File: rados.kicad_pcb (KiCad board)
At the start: 2 copper layers, 156 parts, among them J1 HEADER, J10 STEPSTICK, J11 STEPSTICK, J12 STEPSTICK, J13 MICROSD_SLOT_TFP09-2-12B, J2 HEADER, J3 HEADER, J4 STEPSTICK, J5 STEPSTICK, J6 STEPSTICK, J7 HEADER, J8 HEADER, J9 HEADER, P1 CONN_01X02, P10 CONN_01X04, P11 CONN_01X04, P12 CONN_01X04, P13 EXT_SD, P14 LCD, P15 LIMIT_SWITCHES, P16 LIMIT_SWITCHES_V, P17 CONN_01X03, P18 CONN_01X03, P19 CONN_01X03, P2 CONN_01X02, P20 CONN_01X03, P21 THERMISTORS, P22 CONN_01X05, P3 CONN_01X02, P4 CONN_01X02, P5 HP_MOSFETS, P6 MP_MOSFETS, P7 CONN_02X04, P8 CONN_01X04, P9 CONN_01X04, Q1 2N7002P, Q10 2N7002P, Q11 2N7002P, Q12 BC846BPDW1, Q13 BC846BPDW1, Q14 SI2318CDS-T1-GE3, Q15 IRFB7545PbF, Q16 2N7002P, Q17 2N7002P, Q18 BC846BPDW1, Q19 BC846BPDW1, Q2 2N7002P, Q20 SI2318CDS-T1-GE3, Q21 IRFB7545PbF, Q3 2N7002P, Q4 BC846BPDW1, Q5 BC846BPDW1, Q6 BC846BPDW1, Q7 IRFB7545PbF, Q8 SI2318CDS-T1-GE3, Q9 IRFB7545PbF, SW1 RESET, U1 MC34063, U2 24LC256

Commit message: More routing
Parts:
- added C33: 10uF, Capacitors_SMD:C_0805, F.Cu at (112.5, 140.1)
- C12, C13, C14, C15, C16, C17: footprint geda-footprints:ELCO-8mm -> armin-footprints:ELCO-8mm
- D10, D13, D14, D17, D3, D4, D5, D9: footprint geda-footprints:0603diode -> armin-footprints:0603diode
- D11, D15, D7: footprint geda-footprints:LL-34 -> armin-footprints:LL-34
- D12, D16, D2, D6, D8: footprint geda-footprints:DO214AC -> armin-footprints:DO214AC
- L1: value 100uF -> 100uH
- Q1, Q10, Q11, Q14, Q16, Q17, Q2, Q20, Q3, Q8: footprint geda-footprints:SOT23_3L -> armin-footprints:SOT23_3L
- Q12, Q13, Q18, Q19, Q4, Q5, Q6: footprint geda-footprints:SC70_6L -> armin-footprints:SC70_6L
- Q15, Q21, Q7, Q9: footprint geda-footprints:TO-220 -> armin-footprints:TO-220
- R10: value 1K8 -> 4K7; footprint Resistors_SMD:R_0603 -> Resistors_SMD:R_0805
- U1, U2: footprint geda-footprints:SOIC8 -> armin-footprints:SOIC8
- moved D10 179.5 mm to (96.0, 75.2), turned to 90 degrees
- moved D14 177.1 mm to (96.0, 64.2), turned to 90 degrees
- moved Q17 176.6 mm to (99.0, 65.0), turned to 180 degrees
- moved R23 176.6 mm to (96.2, 71.8), turned to 90 degrees
- moved Q19 174.9 mm to (98.9, 61.4), turned to 180 degrees
- moved R31 173.3 mm to (96.3, 60.9), turned to 90 degrees
- moved Q4 173.2 mm to (98.8, 95.3), turned to 180 degrees
- moved Q11 171.0 mm to (99.0, 76.3), turned to 180 degrees
- moved R29 171.0 mm to (96.2, 67.5), turned to 90 degrees
- moved C5 169.7 mm to (95.9, 56.5), turned to 90 degrees
- moved D3 167.1 mm to (96.0, 97.5), turned to 90 degrees
- moved R27 166.5 mm to (98.9, 59.2)
- moved Q1 165.3 mm to (99.0, 98.2), turned to 180 degrees
- moved C11 161.4 mm to (101.2, 61.2), turned to 90 degrees
- moved R5 161.2 mm to (101.0, 56.5), turned to 270 degrees
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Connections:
- net LCD-5 renamed Net-(SHIELD1-Pad45)
- net LCD-7 renamed Net-(SHIELD1-Pad47)
- J1 pad 2: Net-(J1-Pad2) -> +3V3
- J1 pad 4: Net-(J1-Pad4) -> +3V3
- J1 pad 6: Net-(J1-Pad6) -> +3V3
- J11 pad 1: E1-EN -> E2-EN
- J11 pad 7: E1-STEP -> E2-STEP
- J11 pad 8: E1-DIR -> E2-DIR
- J12 pad 1: E2-EN -> E1-EN
- J12 pad 7: E2-STEP -> E1-STEP
- J12 pad 8: E2-DIR -> E1-DIR
- J2 pad 2: Net-(J2-Pad2) -> +3V3
- J2 pad 4: Net-(J2-Pad4) -> +3V3
- J2 pad 6: Net-(J2-Pad6) -> +3V3
- J3 pad 2: Net-(J3-Pad2) -> +3V3
- J3 pad 4: Net-(J3-Pad4) -> +3V3
- J3 pad 6: Net-(J3-Pad6) -> +3V3
- J4 pad 2: Net-(J1-Pad2) -> Net-(J1-Pad1)
- J4 pad 3: Net-(J1-Pad4) -> Net-(J1-Pad3)
- J4 pad 4: Net-(J1-Pad6) -> Net-(J1-Pad5)
- J5 pad 2: Net-(J2-Pad2) -> Net-(J2-Pad1)
- J5 pad 3: Net-(J2-Pad4) -> Net-(J2-Pad3)
- J5 pad 4: Net-(J2-Pad6) -> Net-(J2-Pad5)
- J6 pad 2: Net-(J3-Pad2) -> Net-(J3-Pad1)
- J6 pad 3: Net-(J3-Pad4) -> Net-(J3-Pad3)
- J6 pad 4: Net-(J3-Pad6) -> Net-(J3-Pad5)
- J7 pad 1: Net-(J7-Pad1) -> Net-(J10-Pad2)
- J7 pad 2: Net-(J10-Pad2) -> +3V3
- J7 pad 3: Net-(J7-Pad3) -> Net-(J10-Pad3)
- J7 pad 4: Net-(J10-Pad3) -> +3V3
- J7 pad 5: Net-(J7-Pad5) -> Net-(J10-Pad4)
- J7 pad 6: Net-(J10-Pad4) -> +3V3
- J8 pad 1: Net-(J8-Pad1) -> Net-(J11-Pad2)
- J8 pad 2: Net-(J11-Pad2) -> +3V3
- J8 pad 3: Net-(J8-Pad3) -> Net-(J11-Pad3)
- J8 pad 4: Net-(J11-Pad3) -> +3V3
- J8 pad 5: Net-(J8-Pad5) -> Net-(J11-Pad4)
- J8 pad 6: Net-(J11-Pad4) -> +3V3
- J9 pad 1: Net-(J9-Pad1) -> Net-(J12-Pad2)
- J9 pad 2: Net-(J12-Pad2) -> +3V3
- J9 pad 3: Net-(J9-Pad3) -> Net-(J12-Pad3)
- J9 pad 4: Net-(J12-Pad3) -> +3V3
- J9 pad 5: Net-(J9-Pad5) -> Net-(J12-Pad4)
- J9 pad 6: Net-(J12-Pad4) -> +3V3
- P17 pad 1: GND -> +3V3
- P17 pad 2: +3V3 -> GND
- P18 pad 1: GND -> +3V3
- P18 pad 2: +3V3 -> GND
- P19 pad 1: GND -> +3V3
- P19 pad 2: +3V3 -> GND
- P20 pad 1: GND -> +3V3
- P20 pad 2: +3V3 -> GND
- R35 pad 1: Net-(R35-Pad1) -> +3V3
- R36 pad 1: Net-(R35-Pad1) -> +3V3
- SHIELD1 pad 0: Y-STEP -> HP-FET3
- SHIELD1 pad 1: Net-(SHIELD1-Pad1) -> Y-STEP
- SHIELD1 pad 15: Net-(SHIELD1-Pad15) -> MP-FET1
- SHIELD1 pad 16: Y-DIR -> LP-FET1
- SHIELD1 pad 17: MP-FET1 -> LP-FET2
- SHIELD1 pad 18: LP-FET2 -> X-STEP
- SHIELD1 pad 19: LP-FET1 -> X-DIR
- SHIELD1 pad 2: Net-(SHIELD1-Pad2) -> Y-DIR
- SHIELD1 pad 22: Y-EN -> X-
- SHIELD1 pad 23: X-DIR -> X+
- SHIELD1 pad 24: X-STEP -> Y-
- SHIELD1 pad 25: Net-(SHIELD1-Pad25) -> Y+
- SHIELD1 pad 26: X-EN -> Z-
- SHIELD1 pad 27: Net-(SHIELD1-Pad27) -> Z+
- SHIELD1 pad 28: X- -> PROBE
- SHIELD1 pad 29: Net-(SHIELD1-Pad29) -> STATUS-LED
- SHIELD1 pad 3: Net-(SHIELD1-Pad3) -> Y-EN
- SHIELD1 pad 30: Y- -> Net-(SHIELD1-Pad30)
- SHIELD1 pad 32: Z- -> Net-(SHIELD1-Pad32)
- SHIELD1 pad 33: Net-(SHIELD1-Pad33) -> LCD-D4
- SHIELD1 pad 34: X+ -> LCD-D7
- SHIELD1 pad 35: Net-(SHIELD1-Pad35) -> LCD-D6
- SHIELD1 pad 36: Y+ -> LCD-E
- SHIELD1 pad 37: Net-(SHIELD1-Pad37) -> LCD-D5
- SHIELD1 pad 38: Z+ -> LCD-RS
- SHIELD1 pad 39: Net-(SHIELD1-Pad39) -> ENC-B
- SHIELD1 pad 40: Net-(SHIELD1-Pad40) -> X-EN
- SHIELD1 pad 41: STATUS-LED -> ENC-A
- SHIELD1 pad 42: LCD-RS -> E3-EN
- SHIELD1 pad 43: LCD-E -> Net-(SHIELD1-Pad43)
- SHIELD1 pad 44: LCD-4 -> E3-STEP
- SHIELD1 pad 46: LCD-6 -> E3-DIR
- SHIELD1 pad 49: E3-EN -> Net-(SHIELD1-Pad49)
- SHIELD1 pad 50: ENC-B -> Net-(SHIELD1-Pad50)
- SHIELD1 pad 51: E3-STEP -> Net-(SHIELD1-Pad51)
- SHIELD1 pad 52: ENC-A -> Net-(SHIELD1-Pad52)
- SHIELD1 pad 53: E3-DIR -> Net-(SHIELD1-Pad53)
- SHIELD1 pad 7: HP-FET3 -> Net-(SHIELD1-Pad7)
- SHIELD1 pad AD0: Net-(SHIELD1-PadAD0) -> E1-DIR
- SHIELD1 pad AD1: Net-(SHIELD1-PadAD1) -> E1-STEP
- SHIELD1 pad AD10: E2-STEP -> AUX-4
- SHIELD1 pad AD11: T4 -> T0
- SHIELD1 pad AD12: T3 -> T1
- SHIELD1 pad AD14: T1 -> T3
- SHIELD1 pad AD15: T0 -> T4
- SHIELD1 pad AD2: Net-(SHIELD1-PadAD2) -> E1-EN
- SHIELD1 pad AD3: Net-(SHIELD1-PadAD3) -> E2-DIR
- SHIELD1 pad AD4: Net-(SHIELD1-PadAD4) -> E2-STEP
- SHIELD1 pad AD6: E1-DIR -> Net-(SHIELD1-PadAD6)
- SHIELD1 pad AD7: E1-STEP -> AUX-1
- SHIELD1 pad AD8: E1-EN -> AUX-2
- SHIELD1 pad AD9: E2-DIR -> AUX-3
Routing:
- net +3V3: track 0.00 -> 373.8 mm
- net +12V: track 26.5 -> 185.7 mm
- net SD2-CS: track 0.00 -> 81.1 mm
- net E1-DIR: track 0.00 -> 61.3 mm
- net E1-STEP: track 0.00 -> 61.1 mm
- net Vsupply: track 261.0 -> 321.8 mm
- net E1-EN: track 0.00 -> 48.5 mm
- net E3-EN: track 0.00 -> 45.3 mm
- net AUX-1: track 0.00 -> 41.6 mm
- net +5V: track 0.00 -> 39.1 mm
- net E2-EN: track 0.00 -> 37.3 mm
- net AUX-2: track 0.00 -> 36.9 mm
- net AUX-3: track 0.00 -> 32.6 mm
- net STATUS-LED: track 0.00 -> 29.2 mm
- net AUX-4: track 0.00 -> 29.2 mm
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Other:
- board outline added: 83 x 106 mm
- net class Default: clearance 0.15 -> 0.1524; trace_width 0.15 -> 0.1524
- rule trace_clearance: 0.15 -> 0.1524
- rule trace_min: 0.15 -> 0.1524

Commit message: Routing almost finished
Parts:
- removed R32, R33, R34: 10K, Resistors_SMD:R_0603
- moved C33 116.4 mm to (92.4, 25.4), turned to 180 degrees
- moved C31 26.7 mm to (149.2, 99.0), turned to 180 degrees
- moved C18 19.5 mm to (142.6, 112.9), turned to 180 degrees
- moved JP2 6.39 mm to (152.3, 105.9), turned to 180 degrees
- moved C32 1.23 mm to (107.0, 106.3)
- moved R42 1.03 mm to (92.8, 27.4), turned to 180 degrees
- moved J13 0.75 mm to (140.0, 118.3)
- moved C30 0.45 mm to (151.4, 33.0)
- moved R6 0.40 mm to (100.8, 89.4)
- moved SW1 0.16 mm to (133.2, 127.5)
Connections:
- C31 pad 2: Net-(C31-Pad2) -> GND
- SHIELD1 pad 1: Y-STEP -> Y-EN
- SHIELD1 pad 3: Y-EN -> Y-STEP
- SHIELD1 pad 42: E3-EN -> Net-(SHIELD1-Pad42)
- SHIELD1 pad 44: E3-STEP -> E3-EN
- SHIELD1 pad 45: Net-(SHIELD1-Pad45) -> E3-STEP
- SHIELD1 pad 48: ENC-SW -> Net-(SHIELD1-Pad48)
- SHIELD1 pad 7: Net-(SHIELD1-Pad7) -> HP-FET1
- SHIELD1 pad 8: HP-FET1 -> Z-STEP
- SHIELD1 pad 9: Z-STEP -> ENC-SW
- SW1 pad 2: Net-(C31-Pad2) -> GND
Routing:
- net +3V3: track 373.8 -> 531.7 mm, vias 0 -> 3
- net SD-CS: track 0.00 -> 77.6 mm
- net Net-(D2-Pad1): track 0.00 -> 71.4 mm
- net RESET: track 0.00 -> 48.9 mm
- net ENC-SW: track 0.00 -> 48.9 mm
- net +12V: track 185.7 -> 230.0 mm
- net SD-SCK: track 48.5 -> 83.9 mm
- net SD-MOSI: track 51.7 -> 86.5 mm, vias 0 -> 1
- net SD-MISO: track 53.1 -> 85.2 mm
- net GND: track 51.7 -> 75.7 mm, vias 22 -> 32
- net ARDUINO-VIN: track 0.00 -> 21.7 mm
- net Z-EN: track 24.5 -> 36.3 mm
- net Y-STEP: track 0.00 -> 5.82 mm
- net Net-(Q7-Pad1): track 0.00 -> 4.89 mm
- net LP-OUT1: track 9.13 -> 13.6 mm
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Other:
- board size 83 x 106 mm -> 83.2 x 106 mm

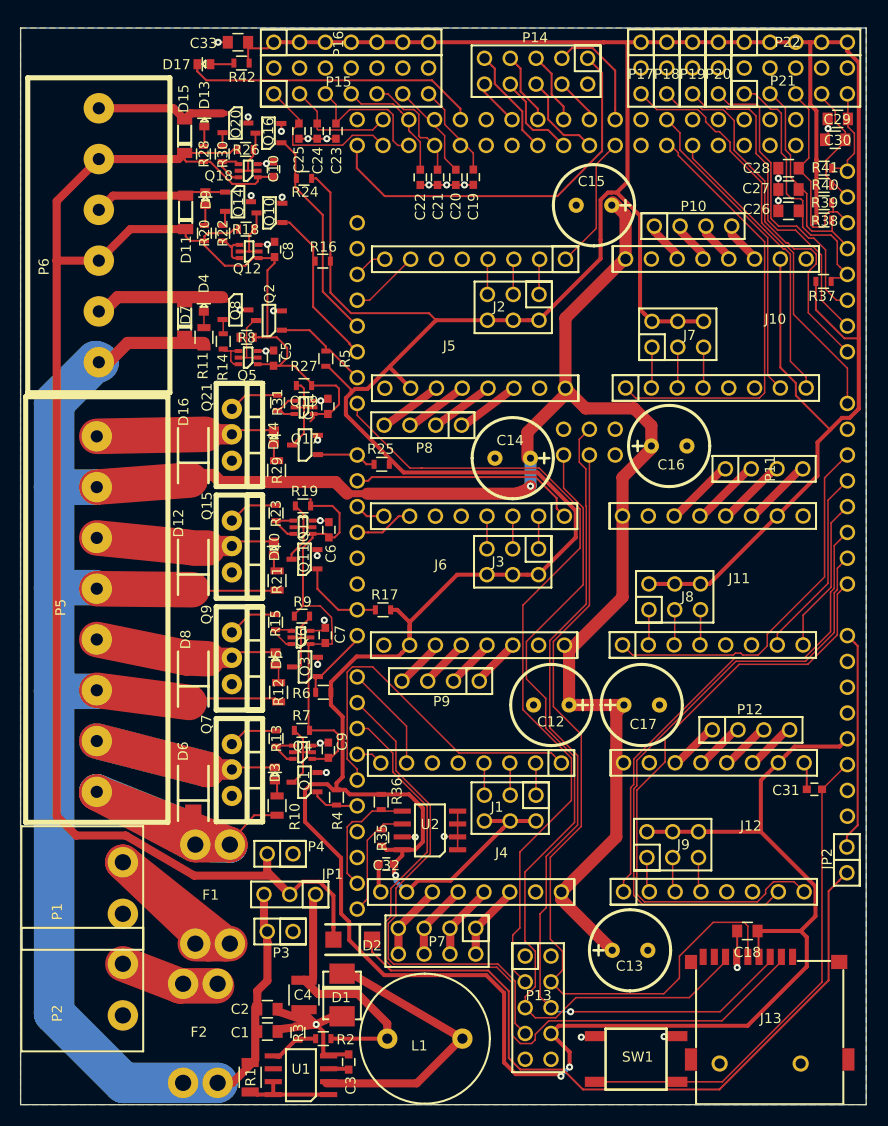
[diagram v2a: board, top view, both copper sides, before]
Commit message: Added 3d models
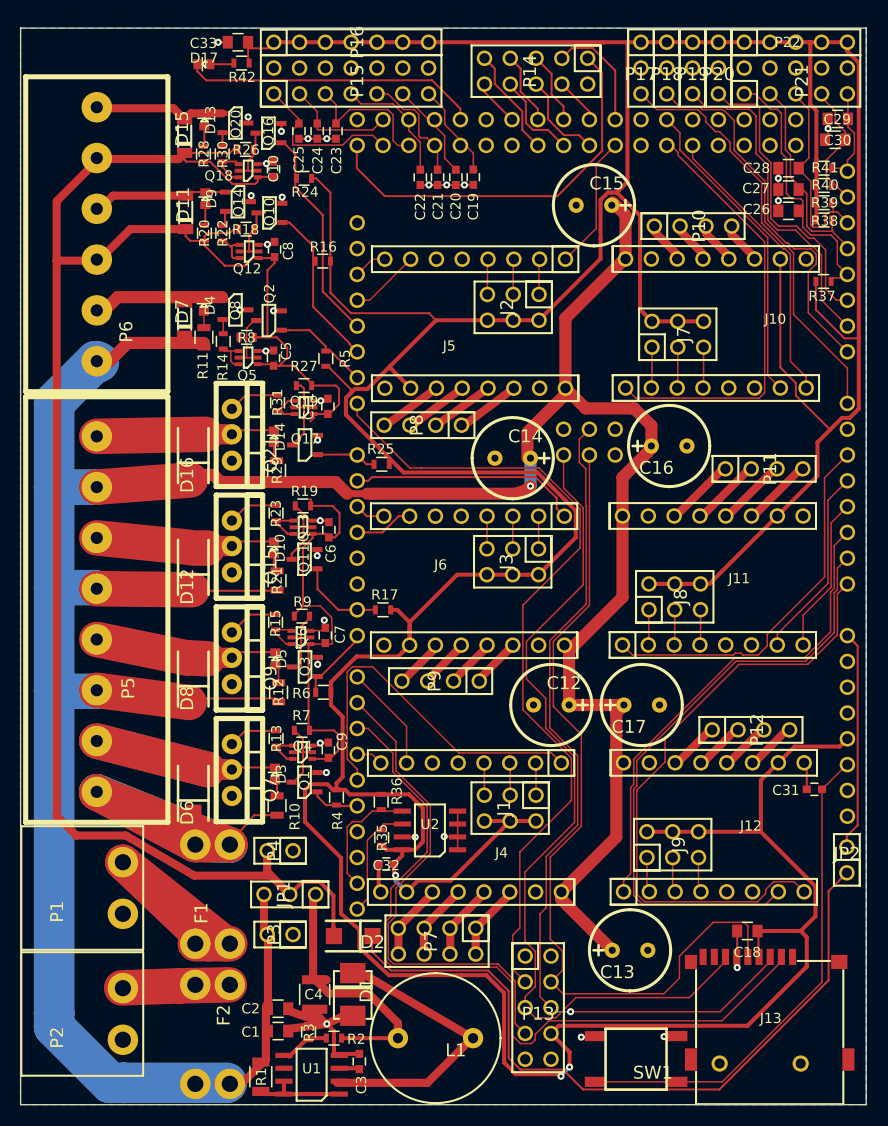
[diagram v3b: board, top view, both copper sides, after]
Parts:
- D1: footprint geda-footprints:SMB -> armin-footprints:DO214AA
- F1, F2: footprint geda-footprints:FUSEHOLDER_MINI_KEYSTONE_3557 -> armin-footprints:FUSEHOLDER_MINI_KEYSTONE_3557
- J1, J2, J3, J7, J8, J9: footprint geda-footprints:CON_HDR_2x3 -> armin-footprints:CON_HDR_2x3_2.54mm
- JP1, P17, P18, P19, P20: footprint geda-footprints:CON_HDR_1x3 -> armin-footprints:CON_HDR_1x3_2.54mm
- JP2, P3, P4: footprint geda-footprints:CON_HDR_1x2 -> armin-footprints:CON_HDR_1x2_2.54mm
- L1: footprint geda-footprints:INDUCTOR_AIUR06 -> armin-footprints:INDUCTOR_AIUR06
- P1, P2: footprint geda-footprints:CON_WURTH_WR_TBL_313_2 -> armin-footprints:CON_PHOENIX_MSTBA-2.5-2-G-5.08
- P10, P11, P12, P8, P9: footprint geda-footprints:CON_HDR_1x4 -> armin-footprints:CON_HDR_1x4_2.54mm
- P13, P14, P21: footprint geda-footprints:CON_HDR_2x5 -> armin-footprints:CON_HDR_2x5_2.54mm
- P15: footprint geda-footprints:CON_HDR_2x7 -> armin-footprints:CON_HDR_2x7_2.54mm
- P16: footprint geda-footprints:CON_HDR_1x7 -> armin-footprints:CON_HDR_1x7_2.54mm
- P5: footprint geda-footprints:CON_SCRW_8_PIN_5mm -> armin-footprints:TERMINAL_BLOCK_8_PIN_5mm
- P6: footprint geda-footprints:CON_SCRW_6_PIN_5mm -> armin-footprints:TERMINAL_BLOCK_6_PIN_5mm
- P7: footprint geda-footprints:CON_HDR_2x4 -> armin-footprints:CON_HDR_2x4_2.54mm
- SW1: footprint geda-footprints:BUTTON_PUSH_SMD_6x6mm -> armin-footprints:BUTTON_PUSH_SMD_6x6mm
- moved P2 2.40 mm to (74.0, 123.4)
- moved F2 1.20 mm to (91.6, 121.2)
- moved R1 1.05 mm to (94.7, 127.2)
- moved U1 1.05 mm to (99.7, 127.0)
- moved R3 1.05 mm to (99.3, 122.8)
- moved C1 1.05 mm to (96.3, 122.8)
- moved C2 1.05 mm to (96.3, 120.5)
- moved C3 1.05 mm to (104.3, 125.8)
- moved C4 1.05 mm to (100.0, 119.2)
- moved D1 1.05 mm to (104.5, 118.8)
- moved L1 1.05 mm to (113.8, 125.2)
- moved R2 1.05 mm to (101.8, 123.5)
- moved D2 0.35 mm to (105.7, 113.4)
- moved P3 0.30 mm to (96.5, 113.2)
- moved P4 0.30 mm to (96.5, 105.0)
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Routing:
- net Vsupply: track 318.9 -> 320.3 mm
- net Net-(F2-Pad1): track 9.63 -> 10.6 mm

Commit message: More 3d stuff
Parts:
- added C34: 10uF, Capacitors_SMD:C_0805, F.Cu at (104.3, 39.1)
- C4: footprint Resistors_SMD:R_1210 -> Capacitors_SMD:C_1210
- J10, J11, J12, J4, J5, J6: footprint geda-footprints:STEPSTICK -> armin-footprints:STEPSTICK
- P22: footprint geda-footprints:CON_HDR_1x5 -> armin-footprints:CON_HDR_1x5_2.54mm
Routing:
- net +5V: track 39.0 -> 39.8 mm, vias 0 -> 1

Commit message: More 3d stuff
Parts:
- C1, C18, C2, C26, C27, C28, C29, C30, C33, C34: footprint Capacitors_SMD:C_0805 -> capacitors:C_0805
- C10, C11, C19, C20, C21, C22, C23, C24, C25, C3, C31, C32, C5, C6, C7, C8, C9: footprint Capacitors_SMD:C_0603 -> capacitors:C_0603
- C12, C13, C14, C15, C16, C17: footprint armin-footprints:ELCO-8mm -> capacitors:ELCO-8mm-3.5mm_pitch
- C4: footprint Capacitors_SMD:C_1210 -> capacitors:C_1210
- D1: footprint armin-footprints:DO214AA -> diodes:DO214AA_SMB
- D10, D13, D14, D17, D3, D4, D5, D9: footprint armin-footprints:0603diode -> diodes:LED-0603
- D11, D15, D7: footprint armin-footprints:LL-34 -> diodes:SOD-80C
- D12, D16, D2, D6, D8: footprint armin-footprints:DO214AC -> diodes:DO214AC_SMA
- F1, F2: footprint armin-footprints:FUSEHOLDER_MINI_KEYSTONE_3557 -> misc:FUSEHOLDER_MINI_KEYSTONE_3557
- L1: footprint armin-footprints:INDUCTOR_AIUR06 -> inductors:INDUCTOR_AIUR06
- P1, P2: footprint armin-footprints:CON_PHOENIX_MSTBA-2.5-2-G-5.08 -> terminal_blocks:CON_PHOENIX_MSTBA-2.5-2-G-5.08
- P5: footprint armin-footprints:TERMINAL_BLOCK_8_PIN_5mm -> terminal_blocks:TERMINAL_BLOCK_8_PIN_5mm
- P6: footprint armin-footprints:TERMINAL_BLOCK_6_PIN_5mm -> terminal_blocks:TERMINAL_BLOCK_6_PIN_5mm
- Q1, Q10, Q11, Q14, Q16, Q17, Q2, Q20, Q3, Q8: footprint armin-footprints:SOT23_3L -> sot:SOT23_3L
- Q12, Q13, Q18, Q19, Q4, Q5, Q6: footprint armin-footprints:SC70_6L -> sot:SC70_6L
- Q15, Q21, Q7, Q9: footprint armin-footprints:TO-220 -> to:TO-220
- R1: footprint Resistors_SMD:R_1206 -> resistors:R_1206
- R10, R11, R12, R21, R29: footprint Resistors_SMD:R_0805 -> resistors:R_0805
- R13, R14, R15, R16, R17, R18, R19, R2, R20, R22, R23, R24, R25, R26, R27, R28, R3, R30, R31, R35, R36, R37, R38, R39, R4, R40, R41, R42, R5, R6, R7, R8, R9: footprint Resistors_SMD:R_0603 -> resistors:R_0603
- SW1: footprint armin-footprints:BUTTON_PUSH_SMD_6x6mm -> buttons_switches:BUTTON_PUSH_SMD_6x6mm
- U1, U2: footprint armin-footprints:SOIC8 -> soic:SOIC8
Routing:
- net +5V: track 39.8 -> 4.98 mm
- net GND: track 75.7 -> 110.5 mm

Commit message: cleanup
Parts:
- Q15, Q21, Q7, Q9: footprint to:TO-220 -> to:TO-220-3

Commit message: fixed minor issue
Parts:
- J1, J2, J3, J7, J8, J9: footprint armin-footprints:CON_HDR_2x3_2.54mm -> headers:CON_HDR_2x3_2.54mm
- JP1, P17, P18, P19, P20: footprint armin-footprints:CON_HDR_1x3_2.54mm -> headers:CON_HDR_1x3_2.54mm
- JP2, P3, P4: footprint armin-footprints:CON_HDR_1x2_2.54mm -> headers:CON_HDR_1x2_2.54mm
- P10, P11, P12, P8, P9: footprint armin-footprints:CON_HDR_1x4_2.54mm -> headers:CON_HDR_1x4_2.54mm
- P13, P14, P21: footprint armin-footprints:CON_HDR_2x5_2.54mm -> headers:CON_HDR_2x5_2.54mm
- P15: footprint armin-footprints:CON_HDR_2x7_2.54mm -> headers:CON_HDR_2x7_2.54mm
- P16: footprint armin-footprints:CON_HDR_1x7_2.54mm -> headers:CON_HDR_1x7_2.54mm
- P22: footprint armin-footprints:CON_HDR_1x5_2.54mm -> headers:CON_HDR_1x5_2.54mm
- P7: footprint armin-footprints:CON_HDR_2x4_2.54mm -> headers:CON_HDR_2x4_2.54mm
- moved C30 0.25 mm to (151.2, 32.9)
- turned C34 to 270 degrees
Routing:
- net GND: track 110.5 -> 76.1 mm, vias 32 -> 33
- net +5V: track 4.98 -> 39.0 mm, vias 1 -> 0

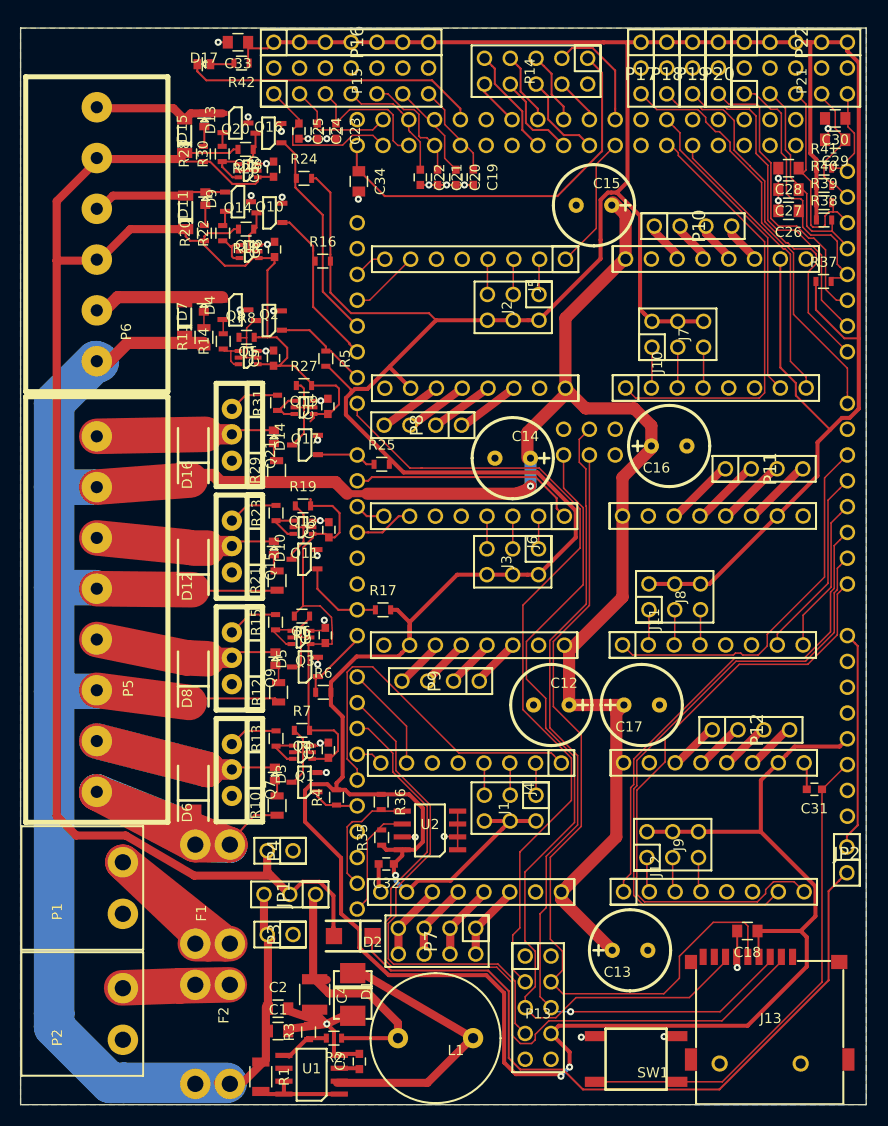
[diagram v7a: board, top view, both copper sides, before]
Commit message: fixed some errors
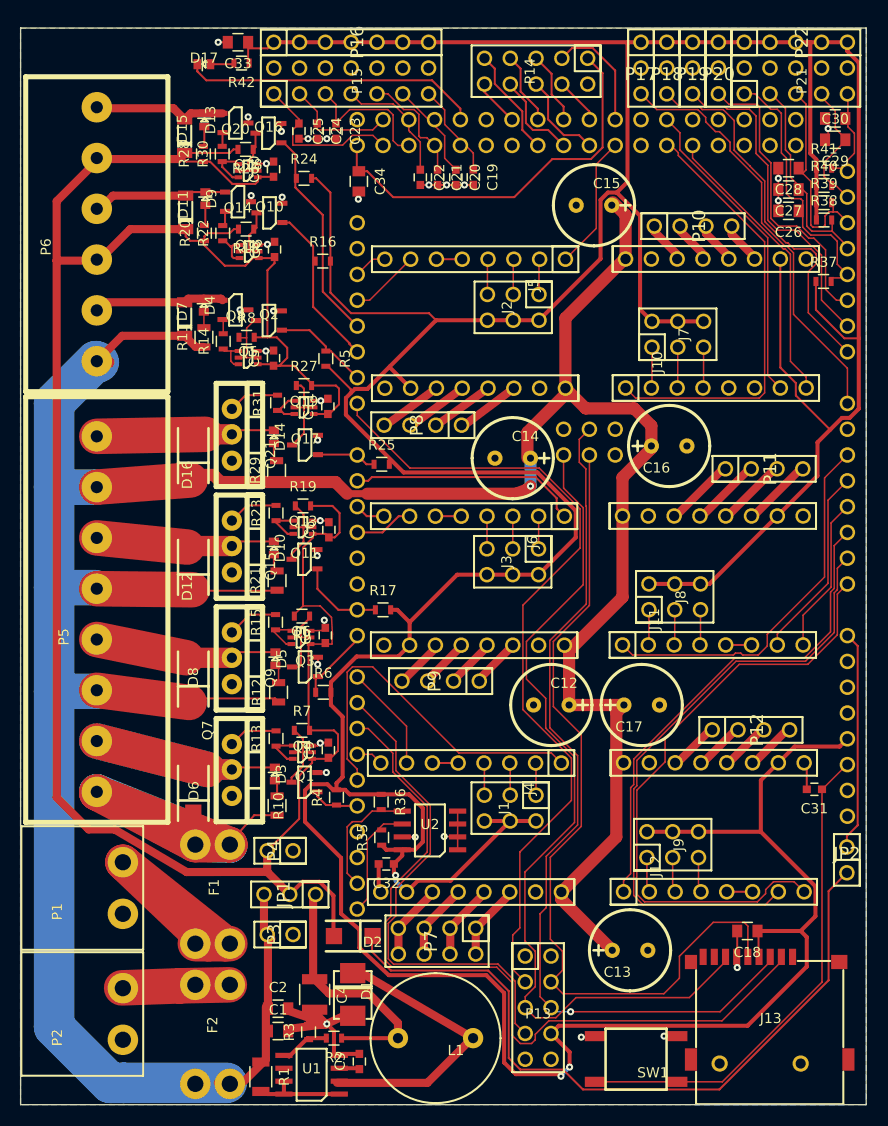
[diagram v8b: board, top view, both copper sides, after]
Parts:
- D11, D15, D7: footprint diodes:SOD-80C -> diodes:DO213AA_SOD-80_MiniMelf
- J10, J11, J12, J4, J5, J6: footprint armin-footprints:STEPSTICK -> misc:STEPSTICK
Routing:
- net +12V: track 230.3 -> 238.0 mm
- net +3V3: track 531.6 -> 528.5 mm
- net Net-(J12-Pad5): track 0.00 -> 2.82 mm
- net Net-(J5-Pad5): track 0.00 -> 2.58 mm
- net Net-(J4-Pad5): track 0.00 -> 2.57 mm
- net Net-(J11-Pad5): track 0.00 -> 2.54 mm
- net Net-(J6-Pad5): track 0.00 -> 2.52 mm
- net HP-OUT1: track 21.5 -> 19.4 mm
- net Vsupply: track 320.3 -> 322.1 mm
- net GND: track 76.1 -> 77.7 mm
- net HP-OUT2: track 18.6 -> 17.2 mm
- net Net-(C4-Pad1): track 26.2 -> 25.3 mm
- net Z+: track 9.63 -> 10.5 mm
- net MP-OUT1: track 12.7 -> 13.4 mm
